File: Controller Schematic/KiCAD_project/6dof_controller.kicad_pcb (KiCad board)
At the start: 2 copper layers, 214.1 x 146.8 mm, 111 parts, among them J1 Screw_Terminal_01x03, J10 Conn_02x13_Top_Bottom, J2 DS-201, J3 RJ45, J4 Conn_02x13_Top_Bottom, J5 Conn_02x13_Top_Bottom, J6 Conn_02x13_Top_Bottom, J7 Conn_02x05_Top_Bottom, J8 Conn_02x13_Top_Bottom, J9 Conn_02x13_Top_Bottom, U1 ESP32_DevKit_V1_DOIT, U10 4N35, U11 4N35, U12 4N35, U13 4N35, U14 4N35, U15 4N35, U2 4N35, U3 MCP23SigIn1M17_SP, U4 4N35, U5 4N35, U6 4N35, U7 4N35, U8 4N35, U9 4N35

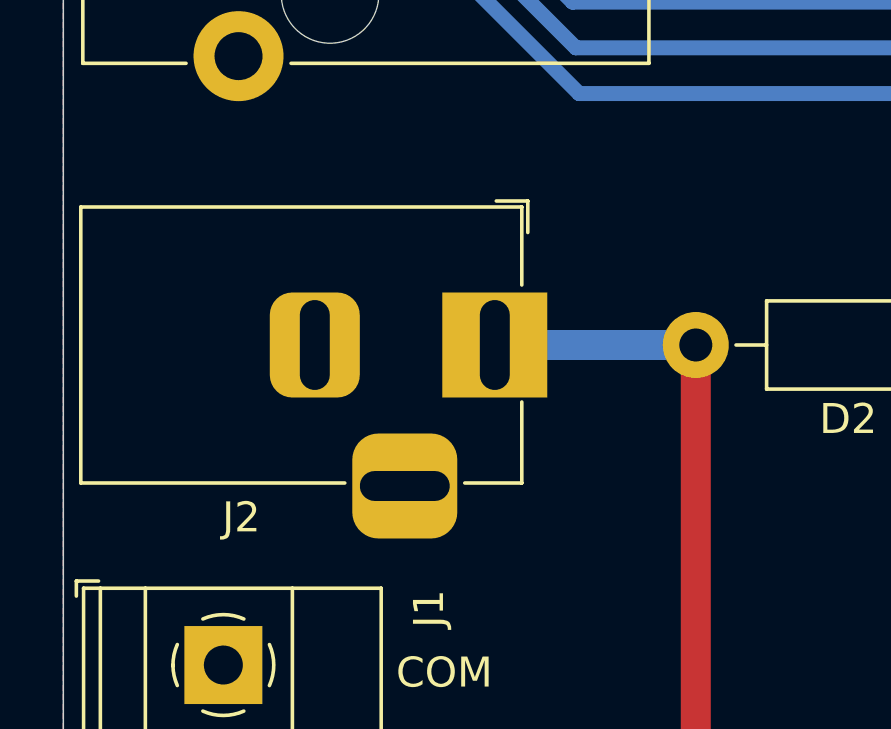
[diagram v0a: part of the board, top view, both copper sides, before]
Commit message: I've renamed folders
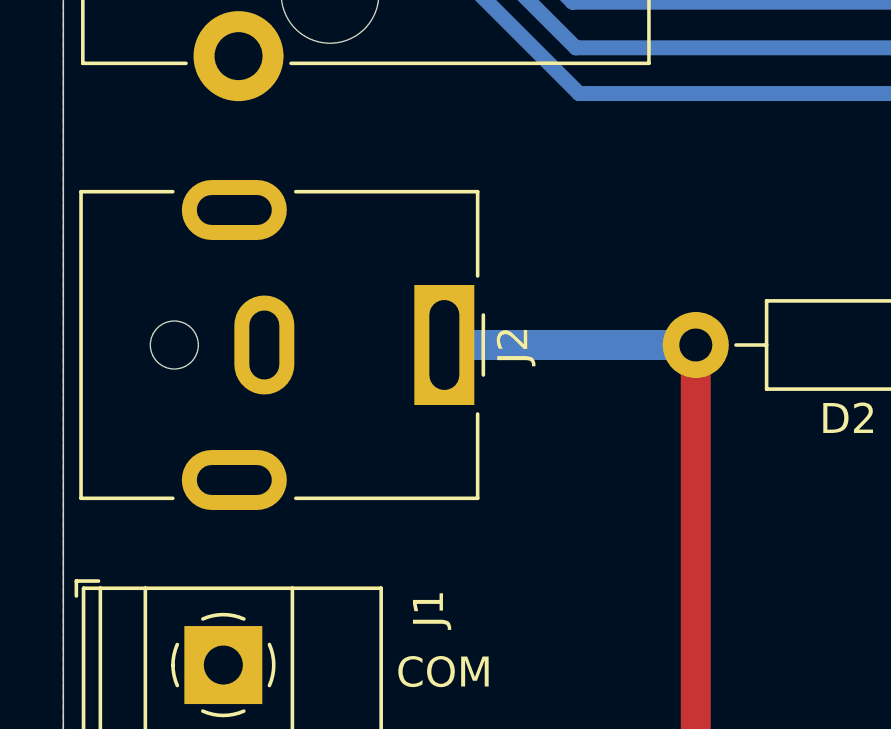
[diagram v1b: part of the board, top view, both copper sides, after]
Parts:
- J2: footprint Connector_BarrelJack:BarrelJack_Horizontal -> Connector_BarrelJack:BarrelJack_CUI_PJ-063AH_Horizontal
- moved J2 1.68 mm to (43.2, 113.8), turned to 270 degrees
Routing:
- net Net-(*J2-Pad1): track 42.8 -> 44.4 mm

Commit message: project updated
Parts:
- added JP4: SolderJumper_2_Open, Jumper:SolderJumper-2_P1.3mm_Open_Pad1.0x1.5mm, B.Cu at (139.3, 61.0)
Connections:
- U3 pad 27: (no net) -> Net-(JP4-Pad1)
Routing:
- net NotSigOut1IN: track 112.7 -> 130.4 mm, vias 2 -> 4
- net Net-(JP4-Pad1): track 0.00 -> 15.4 mm
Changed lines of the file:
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@@
     (thickness 1.6)
     (drawings 199)
-    (tracks 1256)
+    (tracks 1264)
     (zones 0)
-    (modules 111)
-    (nets 103)
+    (modules 112)
+    (nets 104)
   )
   (page A4)
@@
   )
   (setup
-    (last_trace_width 1)
+    (last_trace_width 0.5)
     (user_trace_width 0.5)
     (user_trace_width 1)
@@
   (net 101 "Net-(J1-Pad2)")
   (net 102 "Net-(R15-Pad2)")
+  (net 103 "Net-(JP4-Pad1)")
   (net_class Default "This is the default net class."
     (clearance 0.5)
@@
     (add_net "Net-(JP2-Pad1)")
     (add_net "Net-(JP3-Pad1)")
+    (add_net "Net-(JP4-Pad1)")
     (add_net "Net-(R11-Pad2)")
     (add_net "Net-(R12-Pad2)")
@@
     (add_net "Net-(U3-Pad19)")
     (add_net "Net-(U3-Pad20)")
-    (add_net "Net-(U3-Pad27)")
     (add_net "Net-(U4-Pad3)")
     (add_net "Net-(U4-Pad6)")
@@
   )
   (module Jumper:SolderJumper-2_P1.3mm_Open_Pad1.0x1.5mm (layer B.Cu)
+    (at 139.304 60.96 180)
+    (descr "SMD Solder Jumper, 1x1.5mm Pads, 0.3mm gap, open")
+    (tags "solder jumper open")
+    (attr virtual)
+    (fp_text reference JP4 (at 0 1.8) (layer B.SilkS)
+      (effects (font (size 1 1) (thickness 0.15)) (justify mirror))
+    )
+    (fp_text value SolderJumper_2_Open (at 0 -1.9) (layer B.Fab)
+      (effects (font (size 1 1) (thickness 0.15)) (justify mirror))
+    )
+    (fp_line (start 1.65 -1.25) (end -1.65 -1.25) (layer B.CrtYd) (width 0.05))
+    (fp_line (start 1.65 -1.25) (end 1.65 1.25) (layer B.CrtYd) (width 0.05))
+    (fp_line (start -1.65 1.25) (end -1.65 -1.25) (layer B.CrtYd) (width 0.05))
+    (fp_line (start -1.65 1.25) (end 1.65 1.25) (layer B.CrtYd) (width 0.05))
+    (fp_line (start -1.4 1) (end 1.4 1) (layer B.SilkS) (width 0.12))
+    (fp_line (start 1.4 1) (end 1.4 -1) (layer B.SilkS) (width 0.12))
+    (fp_line (start 1.4 -1) (end -1.4 -1) (layer B.SilkS) (width 0.12))
+    (fp_line (start -1.4 -1) (end -1.4 1) (layer B.SilkS) (width 0.12))
+    (pad 1 smd rect (at -0.65 0 180) (size 1 1.5) (layers B.Cu B.Mask)
+      (net 103 "Net-(JP4-Pad1)"))
+    (pad 2 smd rect (at 0.65 0 180) (size 1 1.5) (layers B.Cu B.Mask)
+      (net 45 NotSigOut1IN))
+  )
+  (module Jumper:SolderJumper-2_P1.3mm_Open_Pad1.0x1.5mm (layer B.Cu)
     (at 139.304 56.896 180)
     (descr "SMD Solder Jumper, 1x1.5mm Pads, 0.3mm gap, open")
@@
     (pad 14 thru_hole oval (at 0 33.02 180) (size 1.6 1.6) (drill 0.8) (layers *.Cu *.Mask)
       (net 34 SO))
-    (pad 27 thru_hole oval (at 7.62 2.54 180) (size 1.6 1.6) (drill 0.8) (layers *.Cu *.Mask))
+    (pad 27 thru_hole oval (at 7.62 2.54 180) (size 1.6 1.6) (drill 0.8) (layers *.Cu *.Mask)
+      (net 103 "Net-(JP4-Pad1)"))
     (pad 13 thru_hole oval (at 0 30.48 180) (size 1.6 1.6) (drill 0.8) (layers *.Cu *.Mask)
       (net 33 SI))
@@
   (segment (start 114.291999 70.366001) (end 122.182001 70.366001) (width 0.5) (layer B.Cu) (net 45))
   (segment (start 56.650001 70.366001) (end 114.291999 70.366001) (width 0.5) (layer B.Cu) (net 45))
+  (via (at 136.906 60.96) (size 1) (drill 0.8) (layers F.Cu B.Cu) (net 45))
+  (segment (start 138.654 60.96) (end 136.906 60.96) (width 0.5) (layer B.Cu) (net 45))
+  (via (at 136.906 70.866) (size 1) (drill 0.8) (layers F.Cu B.Cu) (net 45))
+  (segment (start 136.906 60.96) (end 136.906 70.866) (width 0.5) (layer F.Cu) (net 45))
+  (segment (start 136.906 70.866) (end 130.81 70.866) (width 0.5) (layer B.Cu) (net 45))
   (segment (start 171.5535 132.334) (end 170.434 131.2145) (width 0.5) (layer B.Cu) (net 46))
   (segment (start 175.768 132.334) (end 171.5535 132.334) (width 0.5) (layer B.Cu) (net 46))
@@
   (segment (start 80.01 129.54) (end 80.01 90.471) (width 0.5) (layer F.Cu) (net 101))
   (segment (start 150.368 75.753) (end 150.368 72.898) (width 0.5) (layer F.Cu) (net 102))
+  (segment (start 154.686 59.436) (end 144.78 59.436) (width 0.5) (layer B.Cu) (net 103))
+  (segment (start 143.256 60.96) (end 139.954 60.96) (width 0.5) (layer B.Cu) (net 103))
+  (segment (start 144.78 59.436) (end 143.256 60.96) (width 0.5) (layer B.Cu) (net 103))
   (zone (net 2) (net_name Earth_Protective) (layer F.Cu) (hatch edge 0.508)
     (connect_pads (clearance 0.508))

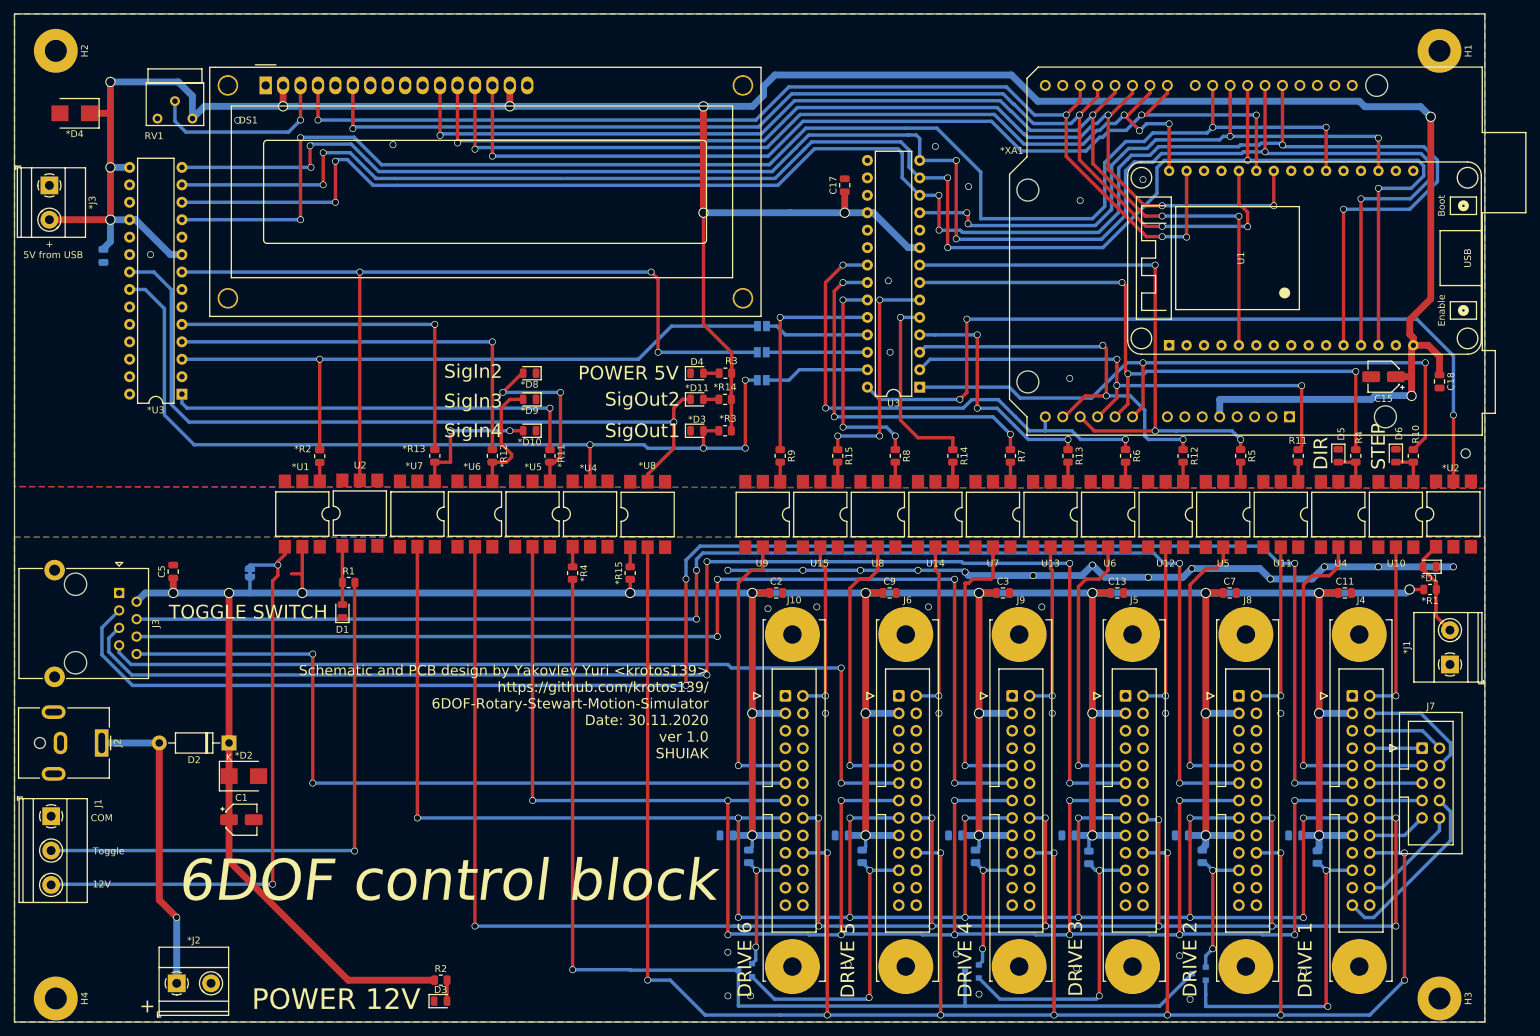
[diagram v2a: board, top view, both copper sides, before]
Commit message: The circuit and board were redesigned after prototyping. Removed all unnecessary. Reduced the PCB.
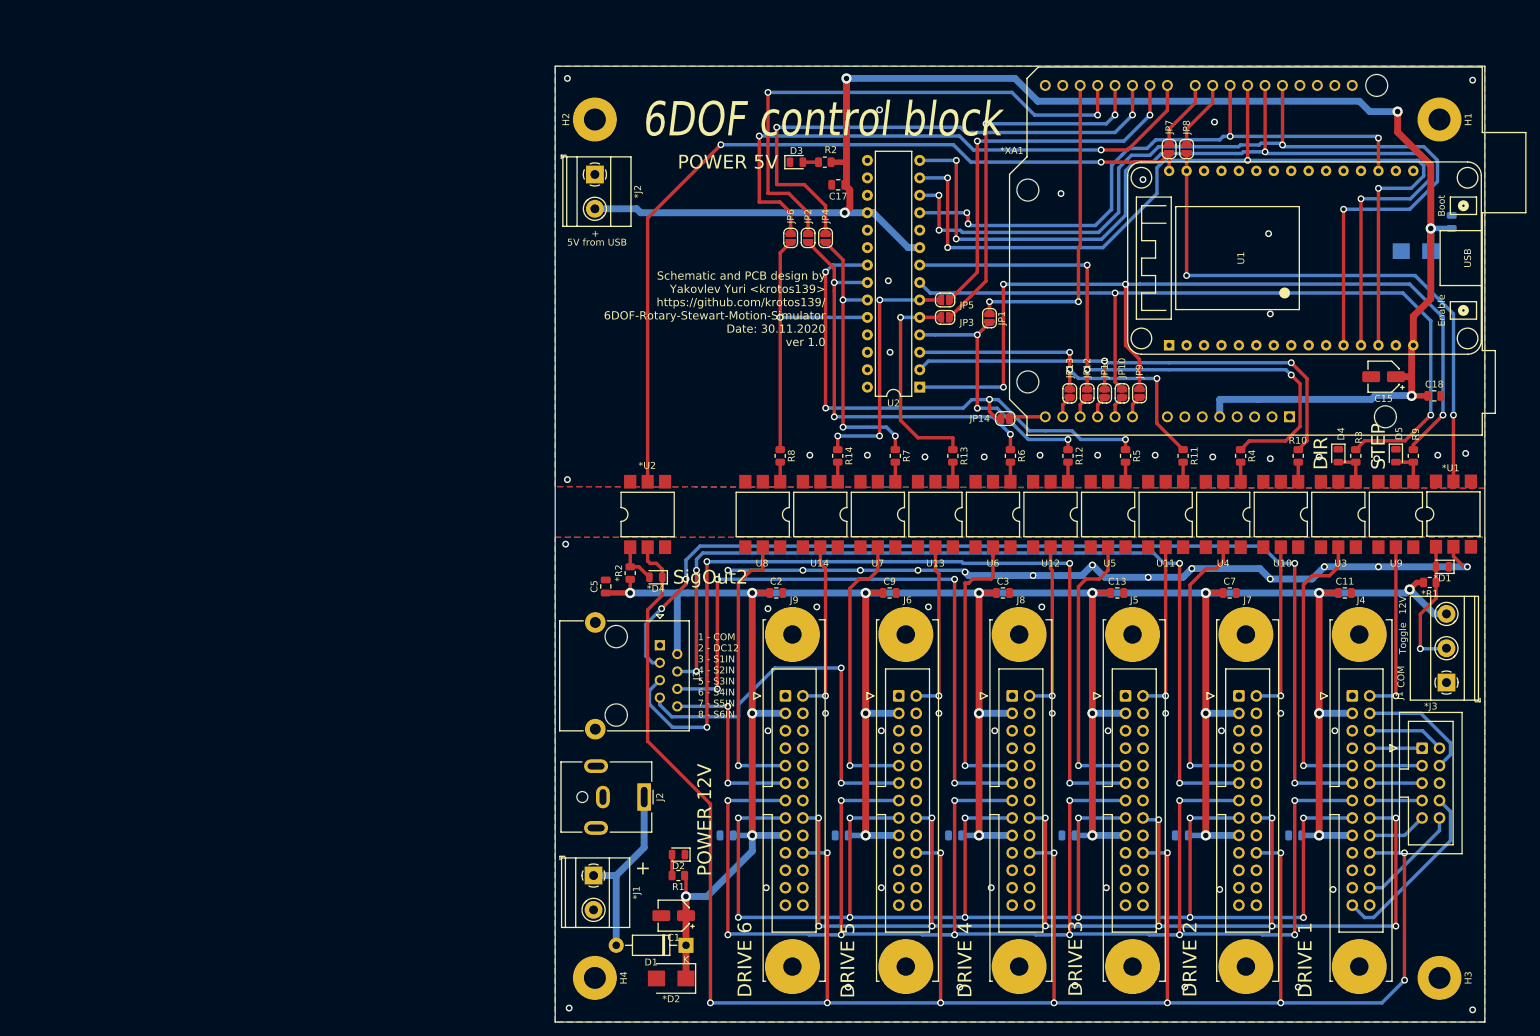
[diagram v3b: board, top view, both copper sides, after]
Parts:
- removed *D10, *D8, *D9: BL-LS0805UYC, LED_SMD:LED_0805_2012Metric
- removed the *D3 at (129.9, 68.3)
- removed *D5, *D6, *D7: BAV23, Package_TO_SOT_SMD:SOT-23
- removed the *J3 at (35.6, 32.6)
- removed *R10, *R14, *R3, *R4, *R5, *R6, *R7, *R8, *R9: 330, Resistor_SMD:R_0805_2012Metric
- removed *R11, *R12, *R13: 100, Resistor_SMD:R_0805_2012Metric
- removed the *R2 at (74.9, 72.0)
- removed the *U1 at (72.4, 80.5)
- removed *U3: MCP23SigIn1M17_SP, Package_DIP:DIP-28_W7.62mm
- removed *U4, *U5, *U6, *U7: 4N35, Package_DIP:SMDIP-6_W9.53mm
- removed the D2 at (61.7, 113.8)
- removed DS1: WC1602A, Display:WC1602A
- removed the R1 at (79.1, 90.4)
- removed RV1: R_POT, Potentiometer_THT:Potentiometer_Bourns_3339W_Horizontal
- removed the U2 at (80.8, 80.3)
- added JP10: SolderJumper_2_Open, Jumper:SolderJumper-2_P1.3mm_Open_RoundedPad1.0x1.5mm, F.Cu at (191.8, 62.9)
- added JP11: SolderJumper_2_Open, Jumper:SolderJumper-2_P1.3mm_Open_RoundedPad1.0x1.5mm, F.Cu at (189.2, 62.9)
- added JP12: SolderJumper_2_Open, Jumper:SolderJumper-2_P1.3mm_Open_RoundedPad1.0x1.5mm, F.Cu at (186.7, 62.9)
- added JP13: SolderJumper_2_Open, Jumper:SolderJumper-2_P1.3mm_Open_RoundedPad1.0x1.5mm, F.Cu at (184.2, 62.9)
- added JP14: SolderJumper_2_Open, Jumper:SolderJumper-2_P1.3mm_Open_RoundedPad1.0x1.5mm, F.Cu at (174.8, 66.5)
- added JP5: SolderJumper_2_Open, Jumper:SolderJumper-2_P1.3mm_Open_RoundedPad1.0x1.5mm, F.Cu at (166.0, 49.3)
- added JP6: SolderJumper_2_Open, Jumper:SolderJumper-2_P1.3mm_Open_RoundedPad1.0x1.5mm, F.Cu at (143.5, 40.2)
- added JP7: SolderJumper_2_Open, Jumper:SolderJumper-2_P1.3mm_Open_RoundedPad1.0x1.5mm, F.Cu at (198.6, 27.3)
- added JP8: SolderJumper_2_Open, Jumper:SolderJumper-2_P1.3mm_Open_RoundedPad1.0x1.5mm, F.Cu at (201.2, 27.3)
- added JP9: SolderJumper_2_Open, Jumper:SolderJumper-2_P1.3mm_Open_RoundedPad1.0x1.5mm, F.Cu at (194.3, 62.9)
- *D3: renamed from *D4; moved to B.Cu
- D1: value BL-LS0805UYC -> 1N4003; footprint LED_SMD:LED_0805_2012Metric -> Diode_THT:D_DO-41_SOD81_P10.16mm_Horizontal
- JP1: value SolderJumper_2_Bridged -> SolderJumper_2_Open; footprint Jumper:SolderJumper-2_P1.3mm_Bridged_RoundedPad1.0x1.5mm -> Jumper:SolderJumper-2_P1.3mm_Open_RoundedPad1.0x1.5mm; moved to F.Cu
- JP2, JP3, JP4: footprint Jumper:SolderJumper-2_P1.3mm_Open_Pad1.0x1.5mm -> Jumper:SolderJumper-2_P1.3mm_Open_RoundedPad1.0x1.5mm; moved to F.Cu
- moved J1 204.1 mm to (239.0, 105.0), turned to 90 degrees
- moved C16 196.4 mm to (239.8, 37.9), turned to 90 degrees
- moved *D3 196.4 mm to (234.6, 42.2)
- moved *J2 132.6 mm to (115.0, 31.0), turned to 270 degrees
- moved *J1 128.4 mm to (114.8, 133.1), turned to 270 degrees
- moved JP1 113.9 mm to (172.5, 51.9), turned to 270 degrees
- moved J2 79.4 mm to (122.2, 121.7)
- moved H2 79.1 mm to (115.0, 23.0), turned to 90 degrees
- moved J3 79.1 mm to (124.5, 99.6)
- moved H4 78.6 mm to (115.0, 148.0)
- moved D1 69.8 mm to (128.3, 143.3), turned to 180 degrees
- moved *D2 68.9 mm to (126.1, 148.1), turned to 180 degrees
- moved C1 64.5 mm to (126.5, 138.9), turned to 180 degrees
- moved C5 63.0 mm to (116.6, 91.0)
- moved D2 40.7 mm to (127.2, 130.0), turned to 180 degrees
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- renumbered *D11 to *D4, J7 to *J3, *R15 to *R2, *U2 to *U1, *U8 to *U2, D3 to D2, D4 to D3, D5 to D4, D6 to D5, J8 to J7, J9 to J8, J10 to J9, R2 to R1, R11 to R10, R12 to R11, R13 to R12, R14 to R13, R15 to R14, R3 to R2, R4 to R3, R5 to R4, R6 to R5, R7 to R6, R8 to R7, R9 to R8, R10 to R9, U11 to U10, U12 to U11, U13 to U12, U14 to U13, U15 to U14, U3 to U2, U4 to U3, U5 to U4, U6 to U5, U7 to U6, U8 to U7, U9 to U8, U10 to U9
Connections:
- *D4 pad 1: SigOut2IN -> SigOut2
- *D4 pad 2: Net-(*D11-Pad2) -> Net-(*D4-Pad2)
- *J1 pad 1: COM -> Net-(*J1-Pad1)
- *J1 pad 2: Net-(*D1-Pad2) -> COM
- *J2 pad 1: Net-(*J2-Pad1) -> Earth_Protective
- *J2 pad 2: COM -> 5V
- *R2 pad 2: Net-(*R15-Pad2) -> Net-(*D4-Pad2)
- *U2 pad 1: Net-(*R15-Pad2) -> Net-(*D4-Pad2)
- *XA1 pad 10: /DirM1 -> Net-(*XA1-Pad10)
- *XA1 pad 11: /StepM2 -> Net-(*XA1-Pad11)
- *XA1 pad 12: /DirM2 -> Net-(*XA1-Pad12)
- *XA1 pad 13: /StepM3 -> Net-(*XA1-Pad13)
- *XA1 pad 14: /DirM3 -> Net-(*XA1-Pad14)
- *XA1 pad 17: LCDD2 -> Net-(*XA1-Pad17)
- *XA1 pad 18: LCDD3 -> Net-(*XA1-Pad18)
- *XA1 pad 19: LCDD4 -> Net-(*XA1-Pad19)
- *XA1 pad 20: LCDD5 -> Net-(*XA1-Pad20)
- *XA1 pad 21: LCDD6 -> Net-(*XA1-Pad21)
- *XA1 pad 22: LCDD7 -> Net-(*XA1-Pad22)
- *XA1 pad 23: (no net) -> Net-(*XA1-Pad23)
- *XA1 pad 24: CSigIn1M1 -> Net-(*XA1-Pad24)
- *XA1 pad 9: /StepM1 -> Net-(*XA1-Pad9)
- D1 pad 1: COM -> DC12
- D1 pad 2: Net-(D1-Pad2) -> Net-(*J1-Pad1)
- J1 pad 2: Net-(J1-Pad2) -> Net-(*D1-Pad2)
- J1 pad 3: Net-(*U1-Pad4) -> DC12
- J2 pad 1: Net-(*J2-Pad1) -> Net-(*J1-Pad1)
- J4 pad 21: SigOut1M1 -> (no net)
- J5 pad 21: SigOut1M3 -> (no net)
- J6 pad 21: SigOut1M5 -> (no net)
- J7 pad 21: SigOut1M2 -> (no net)
- J8 pad 21: SigOut1M4 -> (no net)
- J9 pad 21: SigOut1M6 -> (no net)
- JP1 pad 1: DC12 -> Net-(*XA1-Pad17)
- JP1 pad 2: Net-(*U1-Pad4) -> /StepM4
- JP2 pad 1: Net-(JP2-Pad1) -> Net-(*XA1-Pad18)
- JP2 pad 2: PanelLED -> /DirM4
- JP3 pad 1: Net-(JP3-Pad1) -> Net-(*XA1-Pad19)
- JP3 pad 2: PanelIN -> /StepM5
- JP4 pad 1: Net-(JP4-Pad1) -> Net-(*XA1-Pad20)
- JP4 pad 2: NotSigOut1IN -> /DirM5
- U1 pad 21: CSigIn1M1 -> (no net)
- U1 pad 24: LCDD5 -> (no net)
- U1 pad 25: LCDD7 -> (no net)
- U1 pad 26: LCDD3 -> (no net)
- U1 pad 29: LCDD2 -> BTN1IN
- U1 pad 30: LCDD6 -> SigOut2IN
- U1 pad 5: LCDD4 -> (no net)
- U2 pad 25: Net-(JP2-Pad1) -> (no net)
- U2 pad 26: Net-(JP3-Pad1) -> (no net)
- U2 pad 27: Net-(JP4-Pad1) -> (no net)
- U2 pad 28: BTN1IN -> (no net)
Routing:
- net CSigIn1M1: track 213.6 -> 0.00 mm, vias 4 -> 0
- net 5V: track 428.4 -> 240.9 mm, vias 10 -> 5
- net LCDD3: track 165.6 -> 0.00 mm, vias 4 -> 0
- net LCDD4: track 163.1 -> 0.00 mm, vias 4 -> 0
- net LCDD2: track 160.9 -> 0.00 mm, vias 4 -> 0
- net Net-(*D5-Pad3): track 159.3 -> 0.00 mm, vias 1 -> 0
- net LCDD5: track 153.7 -> 0.00 mm, vias 4 -> 0
- net LCDD7: track 142.0 -> 0.00 mm, vias 3 -> 0
- net LCDD6: track 130.5 -> 0.00 mm, vias 4 -> 0
- net NotSigOut1IN: track 130.4 -> 0.00 mm, vias 4 -> 0
- net PanelIN: track 125.2 -> 0.00 mm, vias 3 -> 0
- net DC12: track 591.3 -> 467.4 mm, vias 23 -> 21
- net SCK: track 259.9 -> 137.7 mm, vias 6 -> 4
- net SI: track 253.4 -> 133.9 mm, vias 6 -> 4
- net SO: track 258.8 -> 140.6 mm, vias 6 -> 4
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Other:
- board size 214.1 x 146.8 mm -> 135.4 x 139.2 mm
- net class 12V: clearance 1 -> 0.8; via_drill 1.2 -> 0.8
- net class Default: via_drill 0.8 -> 0.6
- board text added: "Schematic and PCB design by Yakovlev Yuri <krotos139> https://github.com/krotos139/ 6DOF-Rotary-Stewart-Motion-Simulator Date: 30.11.2020 ver 1.0"
- board text added: "SigOut2IN"
- board text removed: "+12V"
- board text removed: "ADDR 001"
- board text removed: "AlarmResetOut"
- board text removed: "HALL SENSORS"
- board text removed: "Panel IN"
- board text removed: "PanelLed"
- board text removed: "Power 12V"
- board text removed: "S1IN"
- board text removed: "S2IN"
- board text removed: "S3IN"
- board text removed: "S4IN"
- board text removed: "S5IN"
- board text removed: "S6IN"
- board text removed: "SRV-ON OUT"
- board text removed: "Schematic and PCB design by Yakovlev Yuri <krotos139> https://github.com/krotos139/ 6DOF-Rotary-Stewart-Motion-Simulator Date: 30.11.2020 ver 1.0 SHUIAK"
- board text removed: "SigIn2"
- board text removed: "TOGGLE SWITCH"
- board text removed: "The control signal of power supply and ground 9 - DC12~24V 10 - COM Input command signal 6 - SigIn1: REF (hall sensor) 7- SigIn2: 21- SigIn3: 8 - SigIn4: Output command signal. 11 - SigOUT1： 23 - SigOUT2： 12 - SigOUT3： 24 - SigOUT4： Instruction pulse input port PV:open collector input power Instruction pulse can be three different ways to input 1：Instruction direction and pulse input 2： Clockwise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"
- board text removed: "ZPD OUT"
- board text removed: "ZSC OUT"
- board text removed: "lcdD2"
- board text removed: "lcdD3"
- board text removed: "lcdD5"
- board text removed: "lcdD6"
- board text removed: "lcdD7"

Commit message: I've modified schematic and PCB for 6DOF controller
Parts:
- added LOGO1: Logo_Open_Hardware_Large, Symbol:OSHW-Logo2_14.6x12mm_Copper, F.Cu at (119.6, 60.7)
- added REF**: OSHW-Logo2_24.3x20mm_SilkScreen, Symbol:OSHW-Logo2_24.3x20mm_SilkScreen, B.Cu at (129.5, 54.1)
- added REF**: OSHW-Logo2_14.6x12mm_SilkScreen, Symbol:OSHW-Logo2_14.6x12mm_SilkScreen, F.Cu at (119.6, 60.7)
- *D1, *D4, D2, D3, D4, D5: footprint LED_SMD:LED_0805_2012Metric -> LED_SMD:LED_0805_2012Metric_Pad1.15x1.40mm_HandSolder
- R1: value 330 -> 1K
- moved U8 9.14 mm to (130.3, 80.5)
- moved R8 9.14 mm to (132.8, 72.0)
- moved U14 8.38 mm to (139.4, 80.5)
- moved R14 8.38 mm to (142.0, 72.0)
- moved R7 7.62 mm to (151.1, 72.2)
- moved U7 7.62 mm to (148.6, 80.5)
- moved U13 6.86 mm to (157.7, 80.5)
- moved R13 6.86 mm to (160.3, 72.0)
- moved U6 6.10 mm to (166.9, 80.5)
- moved R6 6.10 mm to (169.4, 72.0)
- moved U12 5.33 mm to (176.0, 80.5)
- moved R12 5.33 mm to (178.6, 72.0)
- moved U5 4.57 mm to (185.2, 80.5)
- moved R5 4.57 mm to (187.7, 72.0)
- moved R11 3.82 mm to (196.8, 72.2)
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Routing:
- net /StepM6: track 36.8 -> 45.2 mm
- net /DirM5: track 41.7 -> 35.1 mm, vias 3 -> 1
- net SM5: track 25.2 -> 31.0 mm
- net /StepM5: track 31.2 -> 25.4 mm
- net SM6: track 25.3 -> 30.8 mm
- net /StepM4: track 38.2 -> 32.8 mm
- net /DirM4: track 60.7 -> 56.1 mm
- net /DirM3: track 78.3 -> 73.7 mm
- net SM4: track 25.1 -> 29.4 mm
- net /DirM6: track 43.5 -> 47.3 mm
- net /DirM2: track 90.5 -> 94.2 mm
- net DM3: track 41.6 -> 38.8 mm
- net /StepM2: track 72.9 -> 75.2 mm
- net SM3: track 25.0 -> 27.0 mm
- net DM2: track 41.8 -> 39.7 mm
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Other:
- board text added: "Schematic and PCB design by Yakovlev Yuri <krotos139> https://github.com/krotos139/ 6DOF-Rotary-Stewart-Motion-Simulator Date: 30.11.2020 ver 1.1"
- board text removed: "Schematic and PCB design by Yakovlev Yuri <krotos139> https://github.com/krotos139/ 6DOF-Rotary-Stewart-Motion-Simulator Date: 30.11.2020 ver 1.0"
